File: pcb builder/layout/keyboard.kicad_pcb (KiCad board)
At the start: 2 copper layers, 293.8 x 122.3 mm, 154 parts

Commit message: Doing something in kicad.
IDK. Tried first to make layout on kicad, it was taking ages so decided to try and just add promicro from keebio to pcb builder's already made stuff. But it doesnt want to update it to pcb from schematics soo, gotta figure that out.
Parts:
- moved D_11 69.7 mm to (271.7, 64.0)
- moved D_12 69.7 mm to (290.8, 64.0)
- moved D_49 69.7 mm to (190.8, 121.2)
- moved D_53 69.7 mm to (267.0, 121.2)
- moved D_8 69.7 mm to (214.6, 64.0)
- moved K_52 69.7 mm to (239.4, 120.7)
- moved K_68 69.7 mm to (303.7, 139.7)
- moved D_23 69.7 mm to (214.6, 83.0)
- moved D_26 69.7 mm to (271.7, 83.0)
- moved D_27 69.7 mm to (290.8, 83.0)
- moved D_38 69.7 mm to (238.4, 102.1)
- moved D_41 69.7 mm to (295.5, 102.1)
- moved D_43 69.7 mm to (76.5, 121.2)
- moved D_44 69.7 mm to (95.5, 121.2)
- moved D_45 69.7 mm to (114.6, 121.2)
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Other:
- net class Default removed

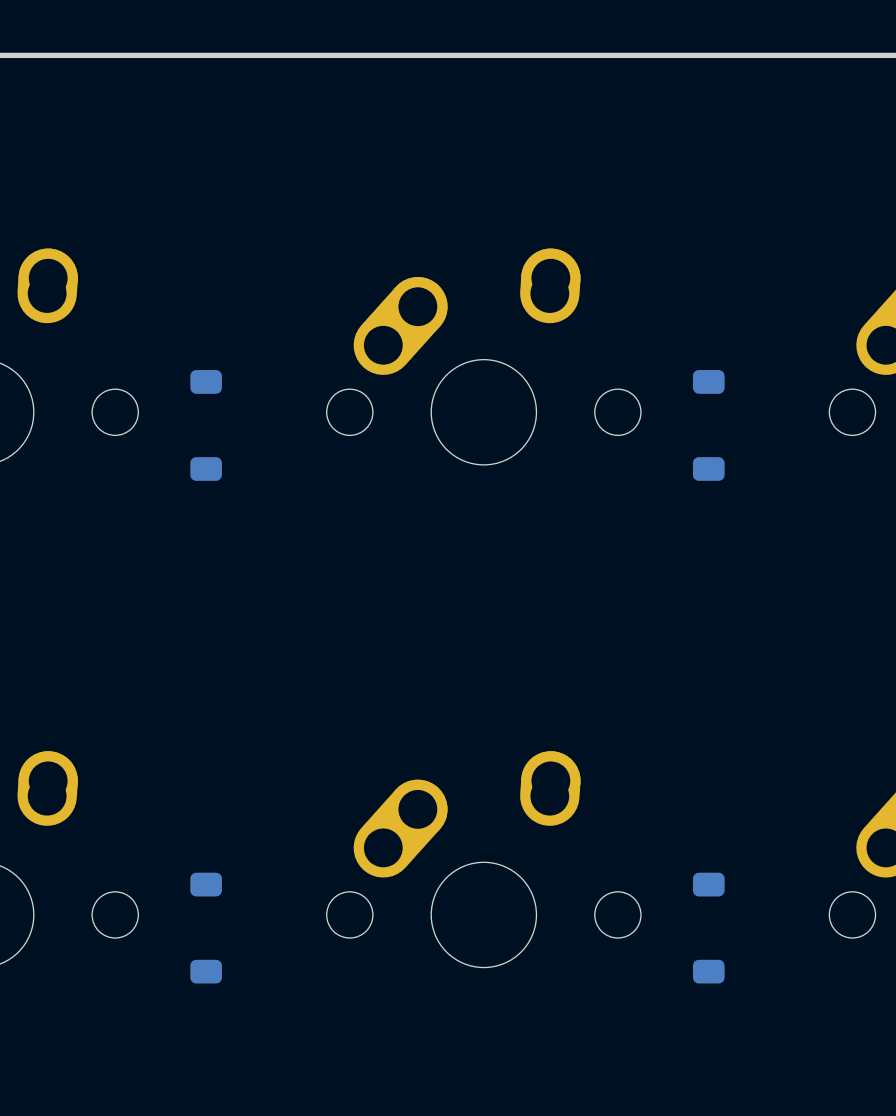
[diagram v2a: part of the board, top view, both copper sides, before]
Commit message: successfully added elite-c
still need to make routes
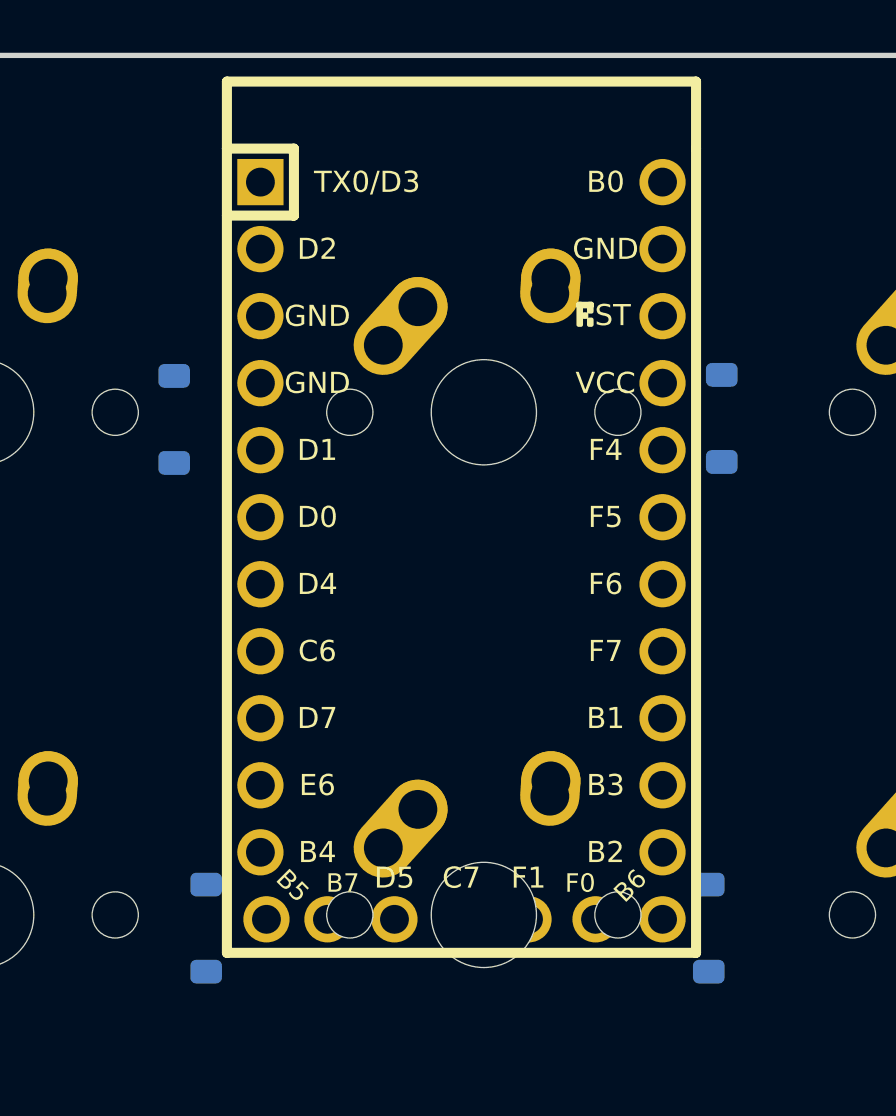
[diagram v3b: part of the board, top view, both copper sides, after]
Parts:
- added U1: Elite-C, Keebio-Parts:Elite-C, F.Cu at (90.9, 68.7)
- moved D_1 1.23 mm to (80.0, 63.8), turned to -90 degrees
- moved D_2 0.56 mm to (100.8, 63.7)

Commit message: rounded pcb corners
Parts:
- moved D_63 0.90 mm to (200.6, 141.0)
- moved K_61 0.90 mm to (154.0, 140.5)
- moved K_66 0.90 mm to (249.3, 140.5)
- moved D_56 0.90 mm to (67.3, 141.0)
- moved K_58 0.90 mm to (96.9, 140.5)
- moved K_59 0.90 mm to (115.9, 140.5)
- moved K_56 0.90 mm to (56.4, 140.5)
- moved D_57 0.90 mm to (86.3, 141.0)
- moved D_58 0.90 mm to (105.4, 141.0)
- moved D_59 0.90 mm to (124.4, 141.0)
- moved D_60 0.90 mm to (143.5, 141.0)
- moved D_61 0.90 mm to (162.5, 141.0)
- moved D_62 0.90 mm to (181.6, 141.0)
- moved D_64 0.90 mm to (219.7, 141.0)
- moved D_65 0.90 mm to (238.7, 141.0)
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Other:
- board size 293.8 x 122.3 mm -> 293.7 x 122.3 mm

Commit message: traced diodes and switches
Need to reposition elite-c and do traces for rows and cols to elite-c.
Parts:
- turned D_1 to 90 degrees
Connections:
- U1 pad 23: unconnected-(U1-GND-Pad23) -> GND
- U1 pad 3: unconnected-(U1-GND-Pad3) -> GND
- U1 pad 4: unconnected-(U1-GND-Pad4) -> GND
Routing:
- net row0: track 0.00 -> 269.9 mm
- net row1: track 0.00 -> 269.1 mm
- net row2: track 0.00 -> 264.3 mm
- net row4: track 0.00 -> 264.1 mm
- net row5: track 0.00 -> 263.2 mm
- net row3: track 0.00 -> 254.6 mm
- net col14: track 0.00 -> 106.9 mm
- net col3: track 0.00 -> 105.4 mm
- net col13: track 0.00 -> 103.5 mm
- net col11: track 0.00 -> 101.6 mm
- net col6: track 0.00 -> 101.6 mm
- net col0: track 0.00 -> 100.9 mm
- net col10: track 0.00 -> 100.6 mm
- net col1: track 0.00 -> 97.3 mm
- net col2: track 0.00 -> 88.7 mm
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
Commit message: retraced everything for promicro.
Thanks Keepo for help. Hope it works now.
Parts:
- removed U1: Elite-C, Keebio-Parts:Elite-C
- added U2: ProMicro, Keebio-Parts:ArduinoProMicro, F.Cu at (91.3, 68.7)
- moved D_17 1.11 mm to (101.7, 84.1)
- moved D_16 0.62 mm to (81.2, 84.3)
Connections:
- K_1 pad 1: col1 -> col0
- K_10 pad 1: col10 -> col5
- K_11 pad 1: col11 -> col5
- K_12 pad 1: col12 -> col6
- K_13 pad 1: col13 -> col6
- K_14 pad 1: col14 -> col7
- K_16 pad 1: col1 -> col0
- K_17 pad 1: col2 -> col1
- K_18 pad 1: col3 -> col1
- K_19 pad 1: col4 -> col2
- K_2 pad 1: col2 -> col1
- K_20 pad 1: col5 -> col2
- K_21 pad 1: col6 -> col3
- K_22 pad 1: col7 -> col3
- K_23 pad 1: col8 -> col4
- K_24 pad 1: col9 -> col4
- K_25 pad 1: col10 -> col5
- K_26 pad 1: col11 -> col5
- K_27 pad 1: col12 -> col6
- K_28 pad 1: col14 -> col7
- K_3 pad 1: col3 -> col1
- K_30 pad 1: col1 -> col0
- K_31 pad 1: col2 -> col1
- K_32 pad 1: col3 -> col1
- K_33 pad 1: col4 -> col2
- K_34 pad 1: col5 -> col2
- K_35 pad 1: col6 -> col3
- K_36 pad 1: col7 -> col3
- K_37 pad 1: col8 -> col4
- K_38 pad 1: col9 -> col4
- K_39 pad 1: col10 -> col5
- K_4 pad 1: col4 -> col2
- K_40 pad 1: col11 -> col5
- K_41 pad 1: col12 -> col6
- K_42 pad 1: col14 -> col7
- K_44 pad 1: col2 -> col1
- K_45 pad 1: col3 -> col1
- K_46 pad 1: col4 -> col2
- K_47 pad 1: col5 -> col2
- K_48 pad 1: col6 -> col3
- K_49 pad 1: col7 -> col3
- K_5 pad 1: col5 -> col2
- K_50 pad 1: col8 -> col4
- K_51 pad 1: col9 -> col4
- K_52 pad 1: col10 -> col5
- K_53 pad 1: col11 -> col5
- K_54 pad 1: col12 -> col6
- K_55 pad 1: col13 -> col6
- K_57 pad 1: col1 -> col0
- K_58 pad 1: col2 -> col1
- K_59 pad 1: col3 -> col1
- K_6 pad 1: col6 -> col3
- K_60 pad 1: col4 -> col2
- K_61 pad 1: col5 -> col2
- K_62 pad 1: col6 -> col3
- K_63 pad 1: col7 -> col3
- K_64 pad 1: col8 -> col4
- K_65 pad 1: col9 -> col4
- K_66 pad 1: col10 -> col5
- K_67 pad 1: col11 -> col5
- K_68 pad 1: col13 -> col6
- K_7 pad 1: col7 -> col3
- K_70 pad 1: col1 -> col0
- K_71 pad 1: col3 -> col1
- K_72 pad 1: col6 -> col3
- K_73 pad 1: col10 -> col5
- K_74 pad 1: col11 -> col5
- K_75 pad 1: col13 -> col6
- K_76 pad 1: col14 -> col7
- K_8 pad 1: col8 -> col4
- K_9 pad 1: col9 -> col4
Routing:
- net col6: track 101.6 -> 397.1 mm, vias 0 -> 2
- net col5: track 83.4 -> 375.7 mm, vias 0 -> 2
- net col7: track 82.5 -> 338.9 mm, vias 0 -> 2
- net col4: track 83.9 -> 294.2 mm, vias 0 -> 2
- net col3: track 105.4 -> 279.5 mm, vias 0 -> 2
- net col0: track 100.9 -> 264.6 mm, vias 0 -> 2
- net col1: track 97.3 -> 239.9 mm
- net col2: track 88.7 -> 219.4 mm
- net col14: track 106.9 -> 0.00 mm
- net col13: track 103.5 -> 0.00 mm
- net col11: track 101.6 -> 0.00 mm
- net col10: track 100.6 -> 0.00 mm
- net col9: track 82.5 -> 0.00 mm
- net col8: track 82.5 -> 0.00 mm
- net col12: track 60.4 -> 0.00 mm
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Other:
- board size 293.7 x 122.3 mm -> 293.5 x 122.2 mm

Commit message: added some mounting holes for m3 screws.
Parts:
- added REF**: MountingHole_3.2mm_M3, MountingHole:MountingHole_3.2mm_M3, F.Cu at (235.3, 53.5)
- added REF**: MountingHole_3.2mm_M3, MountingHole:MountingHole_3.2mm_M3, F.Cu at (139.4, 53.5)
- added REF**: MountingHole_3.2mm_M3, MountingHole:MountingHole_3.2mm_M3, F.Cu at (139.3, 171.2)
- added REF**: MountingHole_3.2mm_M3, MountingHole:MountingHole_3.2mm_M3, F.Cu at (43.3, 171.2)
- added REF**: MountingHole_3.2mm_M3, MountingHole:MountingHole_3.2mm_M3, F.Cu at (43.4, 53.6)
- added REF**: MountingHole_3.2mm_M3, MountingHole:MountingHole_3.2mm_M3, F.Cu at (235.3, 171.2)
- added REF**: MountingHole_3.2mm_M3, MountingHole:MountingHole_3.2mm_M3, F.Cu at (331.5, 53.6)
- added REF**: MountingHole_3.2mm_M3, MountingHole:MountingHole_3.2mm_M3, F.Cu at (331.3, 171.2)
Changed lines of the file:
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@@
       (net 37 "Net-(D_15-A)") (pinfunction "ROW") (pintype "passive"))
   )
+  (footprint "MountingHole:MountingHole_3.2mm_M3" (layer "F.Cu")
+    (at 235.331 53.467)
+    (descr "Mounting Hole 3.2mm, no annular, M3")
+    (tags "mounting hole 3.2mm no annular m3")
+    (attr exclude_from_pos_files exclude_from_bom)
+    (fp_text reference "REF**" (at 0 -4.2) (layer "F.SilkS")
+        (effects (font (size 1 1) (thickness 0.15)))
+    )
+    (fp_text value "MountingHole_3.2mm_M3" (at 0 4.2) (layer "F.Fab")
+        (effects (font (size 1 1) (thickness 0.15)))
+    )
+    (fp_text user "${REFERENCE}" (at 0 0) (layer "F.Fab")
+        (effects (font (size 1 1) (thickness 0.15)))
+    )
+    (fp_circle (center 0 0) (end 3.2 0)
+      (stroke (width 0.15) (type solid)) (fill none) (layer "Cmts.User"))
+    (fp_circle (center 0 0) (end 3.45 0)
+      (stroke (width 0.05) (type solid)) (fill none) (layer "F.CrtYd"))
+    (pad "" np_thru_hole circle (at 0 0) (size 3.2 3.2) (drill 3.2) (layers "F&B.Cu" "*.Mask"))
+  )
   (footprint "MX_Alps_Hybrid:MX-1U-NoLED" (layer "F.Cu")
     (at 206.40625 83.375)
@@
     )
   )
+  (footprint "MountingHole:MountingHole_3.2mm_M3" (layer "F.Cu")
+    (at 139.446 53.467)
+    (descr "Mounting Hole 3.2mm, no annular, M3")
+    (tags "mounting hole 3.2mm no annular m3")
+    (attr exclude_from_pos_files exclude_from_bom)
+    (fp_text reference "REF**" (at 0 -4.2) (layer "F.SilkS")
+        (effects (font (size 1 1) (thickness 0.15)))
+    )
+    (fp_text value "MountingHole_3.2mm_M3" (at 0 4.2) (layer "F.Fab")
+        (effects (font (size 1 1) (thickness 0.15)))
+    )
+    (fp_text user "${REFERENCE}" (at 0 0) (layer "F.Fab")
+        (effects (font (size 1 1) (thickness 0.15)))
+    )
+    (fp_circle (center 0 0) (end 3.2 0)
+      (stroke (width 0.15) (type solid)) (fill none) (layer "Cmts.User"))
+    (fp_circle (center 0 0) (end 3.45 0)
+      (stroke (width 0.05) (type solid)) (fill none) (layer "F.CrtYd"))
+    (pad "" np_thru_hole circle (at 0 0) (size 3.2 3.2) (drill 3.2) (layers "F&B.Cu" "*.Mask"))
+  )
   (footprint "MX_Alps_Hybrid:MX-1U-NoLED" (layer "F.Cu")
     (at 320.70625 64.325)
@@
       (net 72 "Net-(D_50-A)") (pinfunction "ROW") (pintype "passive"))
   )
+  (footprint "MountingHole:MountingHole_3.2mm_M3" (layer "F.Cu")
+    (at 139.319 171.196)
+    (descr "Mounting Hole 3.2mm, no annular, M3")
+    (tags "mounting hole 3.2mm no annular m3")
+    (attr exclude_from_pos_files exclude_from_bom)
+    (fp_text reference "REF**" (at 0 -4.2) (layer "F.SilkS")
+        (effects (font (size 1 1) (thickness 0.15)))
+    )
+    (fp_text value "MountingHole_3.2mm_M3" (at 0 4.2) (layer "F.Fab")
+        (effects (font (size 1 1) (thickness 0.15)))
+    )
+    (fp_text user "${REFERENCE}" (at 0 0) (layer "F.Fab")
+        (effects (font (size 1 1) (thickness 0.15)))
+    )
+    (fp_circle (center 0 0) (end 3.2 0)
+      (stroke (width 0.15) (type solid)) (fill none) (layer "Cmts.User"))
+    (fp_circle (center 0 0) (end 3.45 0)
+      (stroke (width 0.05) (type solid)) (fill none) (layer "F.CrtYd"))
+    (pad "" np_thru_hole circle (at 0 0) (size 3.2 3.2) (drill 3.2) (layers "F&B.Cu" "*.Mask"))
+  )
   (footprint "MX_Alps_Hybrid:MX-1U-NoLED" (layer "F.Cu")
     (at 249.26875 102.425)
@@
       (net 65 "Net-(D_43-A)") (pinfunction "ROW") (pintype "passive"))
   )
+  (footprint "MountingHole:MountingHole_3.2mm_M3" (layer "F.Cu")
+    (at 43.307 171.196)
+    (descr "Mounting Hole 3.2mm, no annular, M3")
+    (tags "mounting hole 3.2mm no annular m3")
+    (attr exclude_from_pos_files exclude_from_bom)
+    (fp_text reference "REF**" (at 0 -4.2) (layer "F.SilkS")
+        (effects (font (size 1 1) (thickness 0.15)))
+    )
+    (fp_text value "MountingHole_3.2mm_M3" (at 0 4.2) (layer "F.Fab")
+        (effects (font (size 1 1) (thickness 0.15)))
+    )
+    (fp_text user "${REFERENCE}" (at 0 0) (layer "F.Fab")
+        (effects (font (size 1 1) (thickness 0.15)))
+    )
+    (fp_circle (center 0 0) (end 3.2 0)
+      (stroke (width 0.15) (type solid)) (fill none) (layer "Cmts.User"))
+    (fp_circle (center 0 0) (end 3.45 0)
+      (stroke (width 0.05) (type solid)) (fill none) (layer "F.CrtYd"))
+    (pad "" np_thru_hole circle (at 0 0) (size 3.2 3.2) (drill 3.2) (layers "*.Cu" "*.Mask"))
+  )
   (footprint "MX_Alps_Hybrid:MX-1U-NoLED" (layer "F.Cu")
     (at 225.45625 83.375)
@@
       (net 74 "Net-(D_52-A)") (pinfunction "ROW") (pintype "passive"))
   )
+  (footprint "MountingHole:MountingHole_3.2mm_M3" (layer "F.Cu")
+    (at 43.434 53.594)
+    (descr "Mounting Hole 3.2mm, no annular, M3")
+    (tags "mounting hole 3.2mm no annular m3")
+    (attr exclude_from_pos_files exclude_from_bom)
+    (fp_text reference "REF**" (at 0 -4.2) (layer "F.SilkS")
+        (effects (font (size 1 1) (thickness 0.15)))
+    )
+    (fp_text value "MountingHole_3.2mm_M3" (at 0 4.2) (layer "F.Fab")
+        (effects (font (size 1 1) (thickness 0.15)))
+    )
+    (fp_text user "${REFERENCE}" (at 0 0) (layer "F.Fab")
+        (effects (font (size 1 1) (thickness 0.15)))
+    )
+    (fp_circle (center 0 0) (end 3.2 0)
+      (stroke (width 0.15) (type solid)) (fill none) (layer "Cmts.User"))
+    (fp_circle (center 0 0) (end 3.45 0)
+      (stroke (width 0.05) (type solid)) (fill none) (layer "F.CrtYd"))
+    (pad "" np_thru_hole circle (at 0 0) (size 3.2 3.2) (drill 3.2) (layers "F&B.Cu" "*.Mask"))
+  )
   (footprint "MX_Alps_Hybrid:MX-1U-NoLED" (layer "F.Cu")
     (at 163.54375 121.475)
@@
       (net 79 "Net-(D_57-A)") (pinfunction "ROW") (pintype "passive"))
   )
+  (footprint "MountingHole:MountingHole_3.2mm_M3" (layer "F.Cu")
+    (at 235.331 171.196)
+    (descr "Mounting Hole 3.2mm, no annular, M3")
+    (tags "mounting hole 3.2mm no annular m3")
+    (attr exclude_from_pos_files exclude_from_bom)
+    (fp_text reference "REF**" (at 0 -4.2) (layer "F.SilkS")
+        (effects (font (size 1 1) (thickness 0.15)))
+    )
+    (fp_text value "MountingHole_3.2mm_M3" (at 0 4.2) (layer "F.Fab")
+        (effects (font (size 1 1) (thickness 0.15)))
+    )
+    (fp_text user "${REFERENCE}" (at 0 0) (layer "F.Fab")
+        (effects (font (size 1 1) (thickness 0.15)))
+    )
+    (fp_circle (center 0 0) (end 3.2 0)
+      (stroke (width 0.15) (type solid)) (fill none) (layer "Cmts.User"))
+    (fp_circle (center 0 0) (end 3.45 0)
+      (stroke (width 0.05) (type solid)) (fill none) (layer "F.CrtYd"))
+    (pad "" np_thru_hole circle (at 0 0) (size 3.2 3.2) (drill 3.2) (layers "F&B.Cu" "*.Mask"))
+  )
   (footprint "MX_Alps_Hybrid:MX-1U-NoLED" (layer "F.Cu")
     (at 268.31875 140.525)
@@
       (net 38 "Net-(D_16-A)") (pinfunction "ROW") (pintype "passive"))
   )
+  (footprint "MountingHole:MountingHole_3.2mm_M3" (layer "F.Cu")
+    (at 331.47 53.594)
+    (descr "Mounting Hole 3.2mm, no annular, M3")
+    (tags "mounting hole 3.2mm no annular m3")
+    (attr exclude_from_pos_files exclude_from_bom)
+    (fp_text reference "REF**" (at 0 -4.2) (layer "F.SilkS")
+        (effects (font (size 1 1) (thickness 0.15)))
+    )
+    (fp_text value "MountingHole_3.2mm_M3" (at 0 4.2) (layer "F.Fab")
+        (effects (font (size 1 1) (thickness 0.15)))
+    )
+    (fp_text user "${REFERENCE}" (at 0 0) (layer "F.Fab")
+        (effects (font (size 1 1) (thickness 0.15)))
+    )
+    (fp_circle (center 0 0) (end 3.2 0)
+      (stroke (width 0.15) (type solid)) (fill none) (layer "Cmts.User"))
+    (fp_circle (center 0 0) (end 3.45 0)
+      (stroke (width 0.05) (type solid)) (fill none) (layer "F.CrtYd"))
+    (pad "" np_thru_hole circle (at 0 0) (size 3.2 3.2) (drill 3.2) (layers "F&B.Cu" "*.Mask"))
+  )
   (footprint "MX_Alps_Hybrid:MX-1U-NoLED" (layer "F.Cu")
     (at 144.49375 121.475)
@@
       (net 39 "Net-(D_17-A)") (pinfunction "ROW") (pintype "passive"))
   )
+  (footprint "MountingHole:MountingHole_3.2mm_M3" (layer "F.Cu")
+    (at 331.343 171.196)
+    (descr "Mounting Hole 3.2mm, no annular, M3")
+    (tags "mounting hole 3.2mm no annular m3")
+    (attr exclude_from_pos_files exclude_from_bom)
+    (fp_text reference "REF**" (at 0 -4.2) (layer "F.SilkS")
+        (effects (font (size 1 1) (thickness 0.15)))
+    )
+    (fp_text value "MountingHole_3.2mm_M3" (at 0 4.2) (layer "F.Fab")
+        (effects (font (size 1 1) (thickness 0.15)))
+    )
+    (fp_text user "${REFERENCE}" (at 0 0) (layer "F.Fab")
+        (effects (font (size 1 1) (thickness 0.15)))
+    )
+    (fp_circle (center 0 0) (end 3.2 0)
+      (stroke (width 0.15) (type solid)) (fill none) (layer "Cmts.User"))
+    (fp_circle (center 0 0) (end 3.45 0)
+      (stroke (width 0.05) (type solid)) (fill none) (layer "F.CrtYd"))
+    (pad "" np_thru_hole circle (at 0 0) (size 3.2 3.2) (drill 3.2) (layers "F&B.Cu" "*.Mask"))
+  )
   (footprint "MX_Alps_Hybrid:MX-1U-NoLED" (layer "F.Cu")

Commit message: filled zone GND
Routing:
- added copper zone on F.Cu, net GND
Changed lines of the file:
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@@
   (segment (start 327.652 155.075) (end 320.825 155.075) (width 0.254) (layer "B.Cu") (net 98))
   (segment (start 327.66 155.067) (end 327.652 155.075) (width 0.254) (layer "B.Cu") (net 98))
+  (zone (net 11) (net_name "GND") (layer "F.Cu") (hatch edge 0.5)
+    (priority 1)
+    (connect_pads (clearance 0.508))
+    (min_thickness 0.25) (filled_areas_thickness no)
+    (fill yes (thermal_gap 0.5) (thermal_bridge_width 0.5))
+    (polygon
+      (pts
+        (xy 331.343 171.196)
+        (xy 43.307 171.196)
+        (xy 43.434 53.594)
+        (xy 331.47 53.594)
+      )
+    )
+  )
 )
